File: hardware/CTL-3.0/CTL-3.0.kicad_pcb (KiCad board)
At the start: 2 copper layers, 106 x 45.1 mm, 63 parts, among them J1 Conn_02x16_Top_Bottom, J2 Conn_02x05_Odd_Even, J3 Conn_01x03, J4 Conn_01x02, J5 Conn_02x06_Odd_Even, J6 Conn_01x04, J7 Conn_01x04, J8 Conn_01x04, K1 G5V-1, Q1 BCX56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

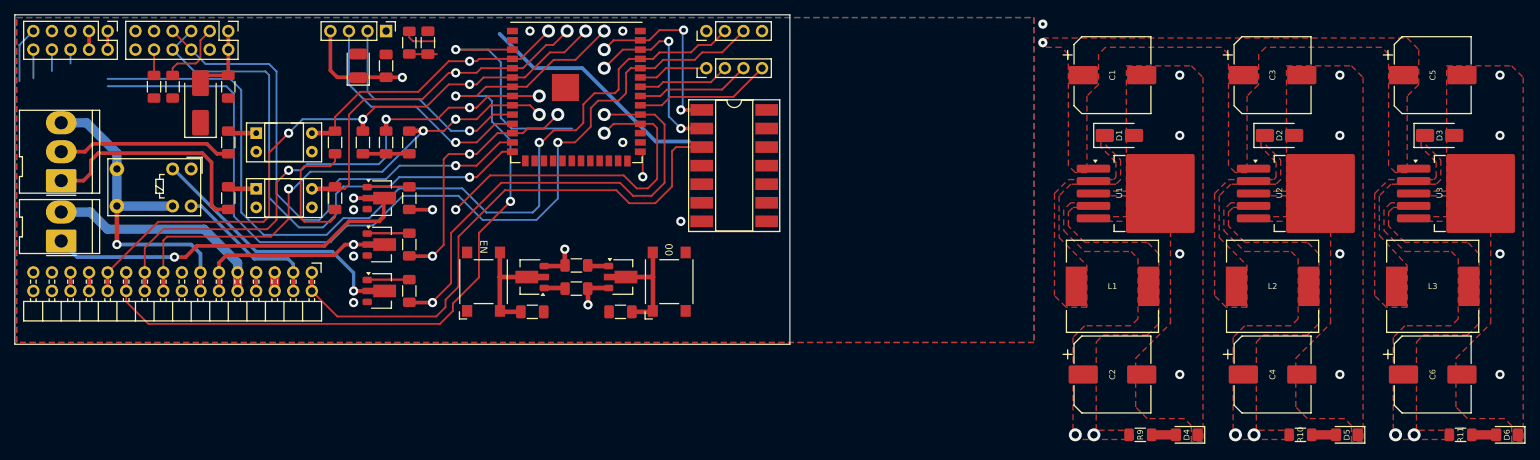
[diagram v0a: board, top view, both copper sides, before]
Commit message: modified:   .DS_Store 	deleted:    hardware/CTL-2.0/CTL-1.0-backups/CTL-1.0-2025-06-05_145506.zip 	deleted:    hardware/CTL-2.0/CTL-1.0-backups/CTL-1.0-2025-06-10_100335.zip 	deleted:    hardware/CTL-2.0/CTL-1.0-backups/CTL-1.0-2025-06-12_095314.zip 	deleted:    hardware/CTL-2.0/CTL-1.0-backups/CTL-1.0-2025-07-03_115731.zip 	deleted:    hardware/CTL-2.0/CTL-1.0-backups/CTL-1.0-2025-07-16_143147.zip 	deleted:    hardware/CTL-2.0/CTL-1.0-backups/CTL-1.0-2025-07-24_151142.zip 	deleted:    hardware/CTL-2.0/CTL-1.0-backups/CTL-1.0-2025-07-24_172002.zip 	deleted:    hardware/CTL-2.0/CTL-1.0-backups/CTL-1.0-2025-07-25_175122.zip 	deleted:    hardware/CTL-2.0/CTL-1.0-backups/CTL-1.0-2025-07-26_120011.zip 	deleted:    hardware/CTL-2.0/CTL-1.0-backups/CTL-1.0-2025-07-26_120808.zip 	deleted:    hardware/CTL-2.0/CTL-1.0-backups/CTL-1.0-2025-07-28_094555.zip 	deleted:    hardware/CTL-2.0/CTL-1.0-backups/CTL-1.0-2025-07-28_104747.zip 	deleted:    hardware/CTL-2.0/CTL-1.0-backups/CTL-1.0-2025-07-28_112613.zip 	deleted:    hardware/CTL-2.0/CTL-1.0-backups/CTL-1.0-2025-07-28_114906.zip 	deleted:    hardware/CTL-2.0/CTL-1.0-backups/CTL-1.0-2025-07-28_120848.zip 	deleted:    hardware/CTL-2.0/CTL-1.0-backups/CTL-1.0-2025-07-29_085804.zip 	deleted:    hardware/CTL-2.0/CTL-1.0-backups/CTL-1.0-2025-07-29_150437.zip 	deleted:    hardware/CTL-2.0/CTL-1.0-backups/CTL-1.0-2025-07-30_093152.zip 	deleted:    hardware/CTL-2.0/CTL-1.0-backups/CTL-1.0-2025-07-31_095618.zip 	deleted:    hardware/CTL-2.0/CTL-1.0-backups/CTL-1.0-2025-08-01_111317.zip 	deleted:    hardware/CTL-2.0/CTL-1.0-backups/CTL-1.0-2025-08-01_113544.zip 	deleted:    hardware/CTL-2.0/CTL-1.0-backups/CTL-1.0-2025-08-01_114559.zip 	deleted:    hardware/CTL-2.0/CTL-1.0-backups/CTL-1.0-2025-08-01_115359.zip 	deleted:    hardware/CTL-2.0/CTL-1.0-backups/CTL-1.0-2025-08-01_115915.zip 	deleted:    hardware/CTL-2.0/CTL-1.0-backups/CTL-1.0-2025-08-01_131607.zip 	deleted:    hardware/CTL-2.0/CTL-1.2-TopSilkscreen.png 	deleted:    hardware/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
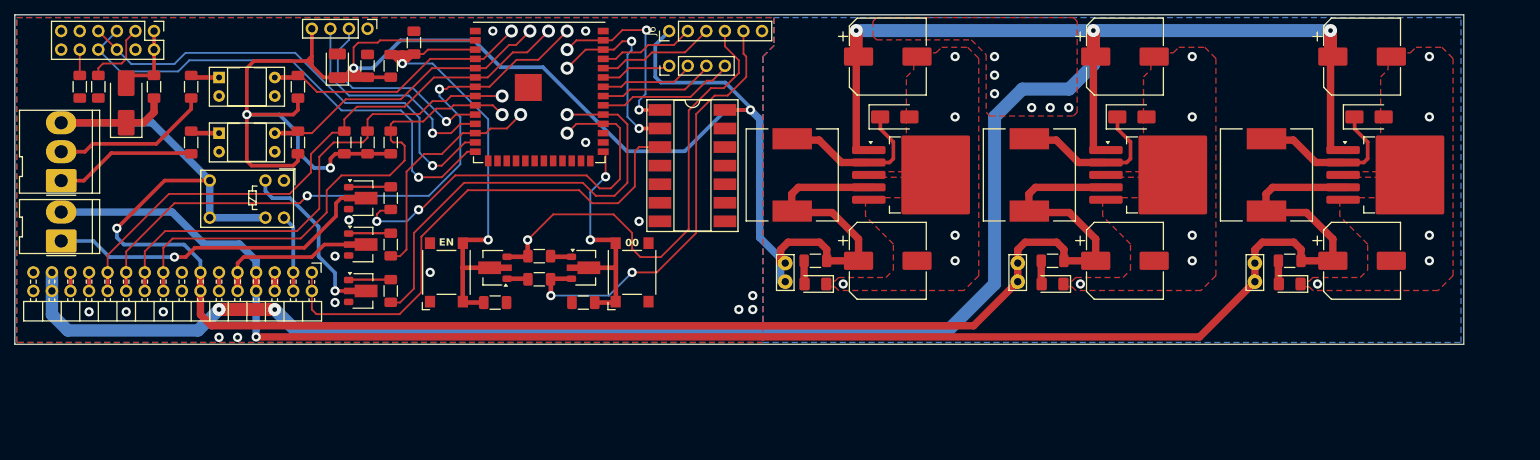
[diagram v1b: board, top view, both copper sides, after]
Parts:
- removed J2: Conn_02x05_Odd_Even, Connector_PinHeader_2.54mm:PinHeader_2x05_P2.54mm_Vertical
- added TP1: TestPoint, TestPoint:TestPoint_Bridge_Pitch2.54mm_Drill1.0mm, F.Cu at (137.2, 150.2)
- added TP2: TestPoint, TestPoint:TestPoint_Bridge_Pitch2.54mm_Drill1.0mm, F.Cu at (169.0, 150.2)
- added TP3: TestPoint, TestPoint:TestPoint_Bridge_Pitch2.54mm_Drill1.0mm, F.Cu at (201.4, 150.2)
- J6: footprint Connector_PinHeader_2.54mm:PinHeader_1x04_P2.54mm_Vertical -> Connector_PinHeader_2.54mm:PinHeader_1x06_P2.54mm_Vertical
- moved D4 54.8 mm to (141.3, 150.5)
- moved R9 50.4 mm to (141.3, 147.3), turned to 180 degrees
- moved L1 46.4 mm to (138.1, 135.6), turned to -90 degrees
- moved D5 45.2 mm to (173.7, 150.5)
- moved R10 41.4 mm to (173.7, 147.3), turned to 180 degrees
- moved L2 36.6 mm to (170.6, 135.6), turned to -90 degrees
- moved D6 36.2 mm to (206.2, 150.5)
- moved C2 34.5 mm to (151.2, 147.3)
- moved R11 33.4 mm to (206.2, 147.3), turned to 180 degrees
- moved C1 30.8 mm to (151.2, 119.4)
- moved U1 30.8 mm to (156.2, 135.6)
- moved D1 30.8 mm to (152.1, 127.6)
- moved L3 27.4 mm to (203.0, 135.6), turned to -90 degrees
- moved C4 25.5 mm to (183.6, 147.3)
- moved C3 20.4 mm to (183.6, 119.4)
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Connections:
- J1 pad 10: +12V -> /RLY-K
- J1 pad 11: /RLY-K -> Net-(J1-Pin_11)
- J1 pad 12: /RLY-K -> Net-(J1-Pin_11)
- J1 pad 7: Net-(J1-Pin_7) -> +12V
- J1 pad 8: Net-(J1-Pin_7) -> +12V
- J1 pad 9: +12V -> /RLY-K
- J6 pad 4: GND -> /RTS
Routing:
- net +24V: track 0.00 -> 297.9 mm, vias 1 -> 5
- net +5V: track 49.0 -> 250.0 mm, vias 3 -> 1
- net +12V: track 30.9 -> 225.3 mm, vias 2 -> 1
- net +3.3V: track 80.2 -> 265.9 mm, vias 3 -> 4
- net /TXD.0: track 125.6 -> 13.1 mm, vias 1 -> 0
- net /RXD.0: track 128.0 -> 16.2 mm, vias 1 -> 0
- net /RTS: track 8.05 -> 65.6 mm
- net /DTR: track 7.03 -> 60.2 mm, vias 1 -> 2
- net /REM: track 113.0 -> 88.3 mm
- net Net-(D3-K): track 0.00 -> 21.2 mm
- net Net-(D1-K): track 0.00 -> 21.2 mm
- net Net-(D2-K): track 0.00 -> 21.2 mm
- net /EN: track 53.3 -> 68.7 mm, vias 1 -> 2
- net /SW-COAG: track 32.1 -> 19.3 mm
- net Net-(Q5-C): track 35.1 -> 22.4 mm
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- removed copper zone on F.Cu, net +12V
- removed copper zone on F.Cu, net +24V
- removed copper zone on F.Cu, net +3.3V
- removed copper zone on F.Cu, net +5V
- removed copper zone on F.Cu, net Net-(D1-K)
- removed copper zone on F.Cu, net Net-(D2-K)
- removed copper zone on F.Cu, net Net-(D3-K)
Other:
- board size 106 x 45.1 mm -> 198.2 x 45.1 mm

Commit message: modified:   .DS_Store 	modified:   README.md 	new file:   hardware/CTL-3.0/CTL-3.0-backups/CTL-3.0-2025-08-08_093936.zip 	new file:   hardware/CTL-3.0/CTL-3.0-backups/CTL-3.0-2025-08-08_103359.zip 	new file:   hardware/CTL-3.0/CTL-3.0-backups/CTL-3.0-2025-08-08_104842.zip 	new file:   hardware/CTL-3.0/CTL-3.0-backups/CTL-3.0-2025-08-08_105743.zip 	modified:   hardware/CTL-3.0/CTL-3.0.kicad_pcb 	modified:   hardware/CTL-3.0/CTL-3.0.kicad_sch 	modified:   hardware/CTL-3.0/CTL-3.0.step 	modified:   hardware/CTL-3.0/fp-info-cache 	modified:   hardware/MSD-1.0/MSD-1.0.step 	deleted:    hardware/PS-2.0/PS-2.0-backups/PS-2.0-2025-07-28_091511.zip 	deleted:    hardware/PS-2.0/PS-2.0-backups/PS-2.0-2025-07-28_120953.zip 	deleted:    hardware/PS-2.0/PS-2.0-backups/PS-2.0-2025-07-29_151613.zip 	deleted:    hardware/PS-2.0/PS-2.0-backups/PS-2.0-2025-07-30_104542.zip 	deleted:    hardware/PS-2.0/PS-2.0-backups/PS-2.0-2025-08-07_142024.zip 	new file:   hardware/PS-2.0/PS-2.0-backups/PS-2.0-2025-08-08_083444.zip 	new file:   hardware/PS-2.0/PS-2.0-backups/PS-2.0-2025-08-08_093021.zip 	new file:   hardware/PS-2.0/PS-2.0-backups/PS-2.0-2025-08-08_095017.zip 	new file:   hardware/PS-2.0/PS-2.0-backups/PS-2.0-2025-08-08_101231.zip 	new file:   hardware/PS-2.0/PS-2.0-backups/PS-2.0-2025-08-08_102520.zip 	modified:   hardware/PS-2.0/PS-2.0.kicad_pcb 	modified:   hardware/PS-2.0/PS-2.0.kicad_prl 	new file:   hardware/PS-2.0/~PS-2.0.kicad_pcb.lck 	modified:   hardware/REM-4.0/REM-4.0.step 	deleted:    hardware/XF-1.0/XF-1.0-backups/XF-1.0-2025-07-17_151907.zip 	deleted:    hardware/XF-1.0/XF-1.0-backups/XF-1.0-2025-08-07_145812.zip 	new file:   hardware/XF-1.0/XF-1.0-backups/XF-1.0-2025-08-08_083643.zip 	new file:   hardware/XF-1.0/XF-1.0-backups/XF-1.0-2025-08-08_100854.zip 	new file:   hardware/XF-1.0/XF-1.0-backups/XF-1.0-2025-08-08_101915.zip 	modified:   hardware/XF-1.0/XF-1.0.kicad_pcb 	modified:   hardware/XF-1.0/XF-1.0.step 	modified:   hardware/XF-1.0/fp-info-cache 	modified:   l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
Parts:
- C1, C3, C5: value 100µF 35V -> 100µF 50V
- moved J3 7.92 mm to (38.1, 128.4), turned to -90 degrees
- moved J4 3.96 mm to (38.1, 140.7), turned to -90 degrees
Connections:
- J3 pad 1: /SW-COAG -> +5V
- J3 pad 3: +5V -> /SW-COAG
- J4 pad 1: /BUZZ -> +12V
- J4 pad 2: +12V -> /BUZZ
